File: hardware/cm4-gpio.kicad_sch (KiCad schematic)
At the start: 1 part, among them J2 DF40C-100DP-0.4V_51_

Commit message: Adding SDRAM - missing 3 pins
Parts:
- J2: footprint apparillo-lib:HRS_DF40C-100DP-0.4V_51_ -> ulx5m-gs:HRS_DF40C-100DP-0.4V_51_
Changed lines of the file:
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@@
 			)
 		)
-		(property "Footprint" "apparillo-lib:HRS_DF40C-100DP-0.4V_51_"
+		(property "Footprint" "ulx5m-gs:HRS_DF40C-100DP-0.4V_51_"
 			(at 152.4 88.9 0)
 			(effects

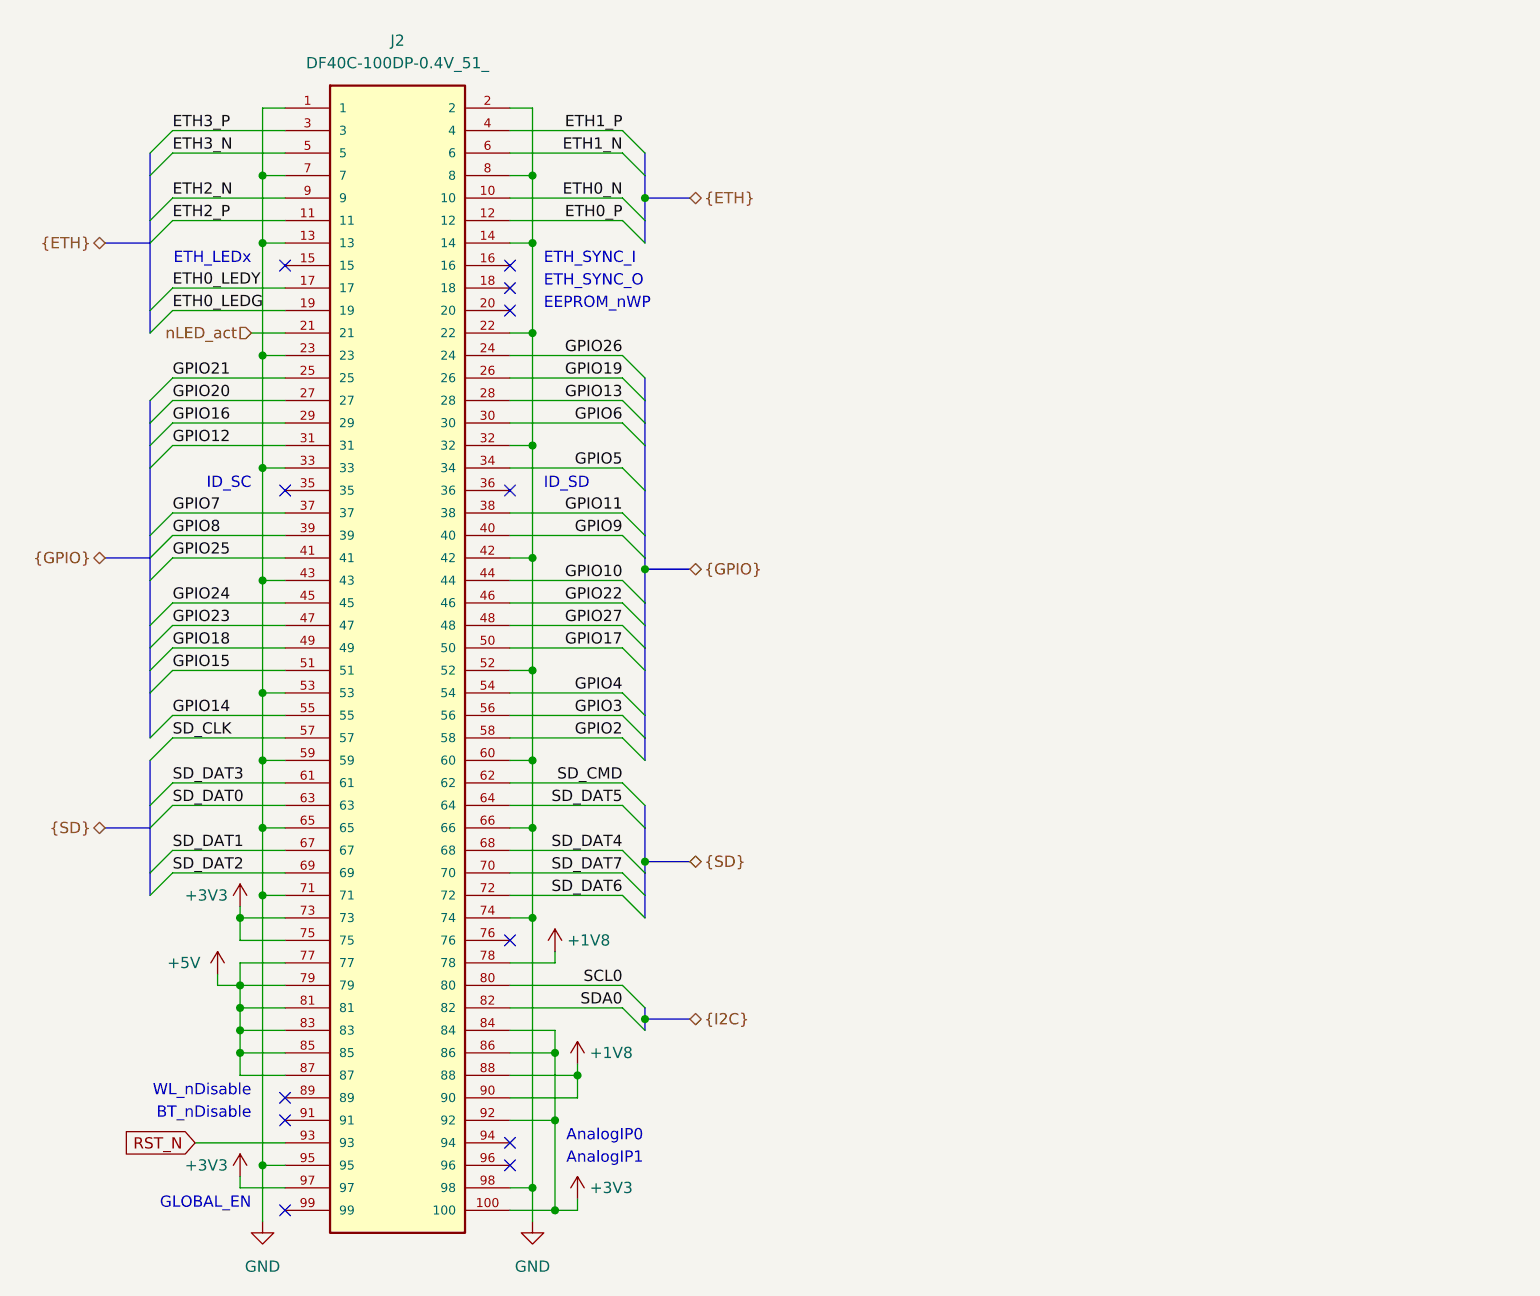
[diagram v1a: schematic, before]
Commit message: Routing diff clock
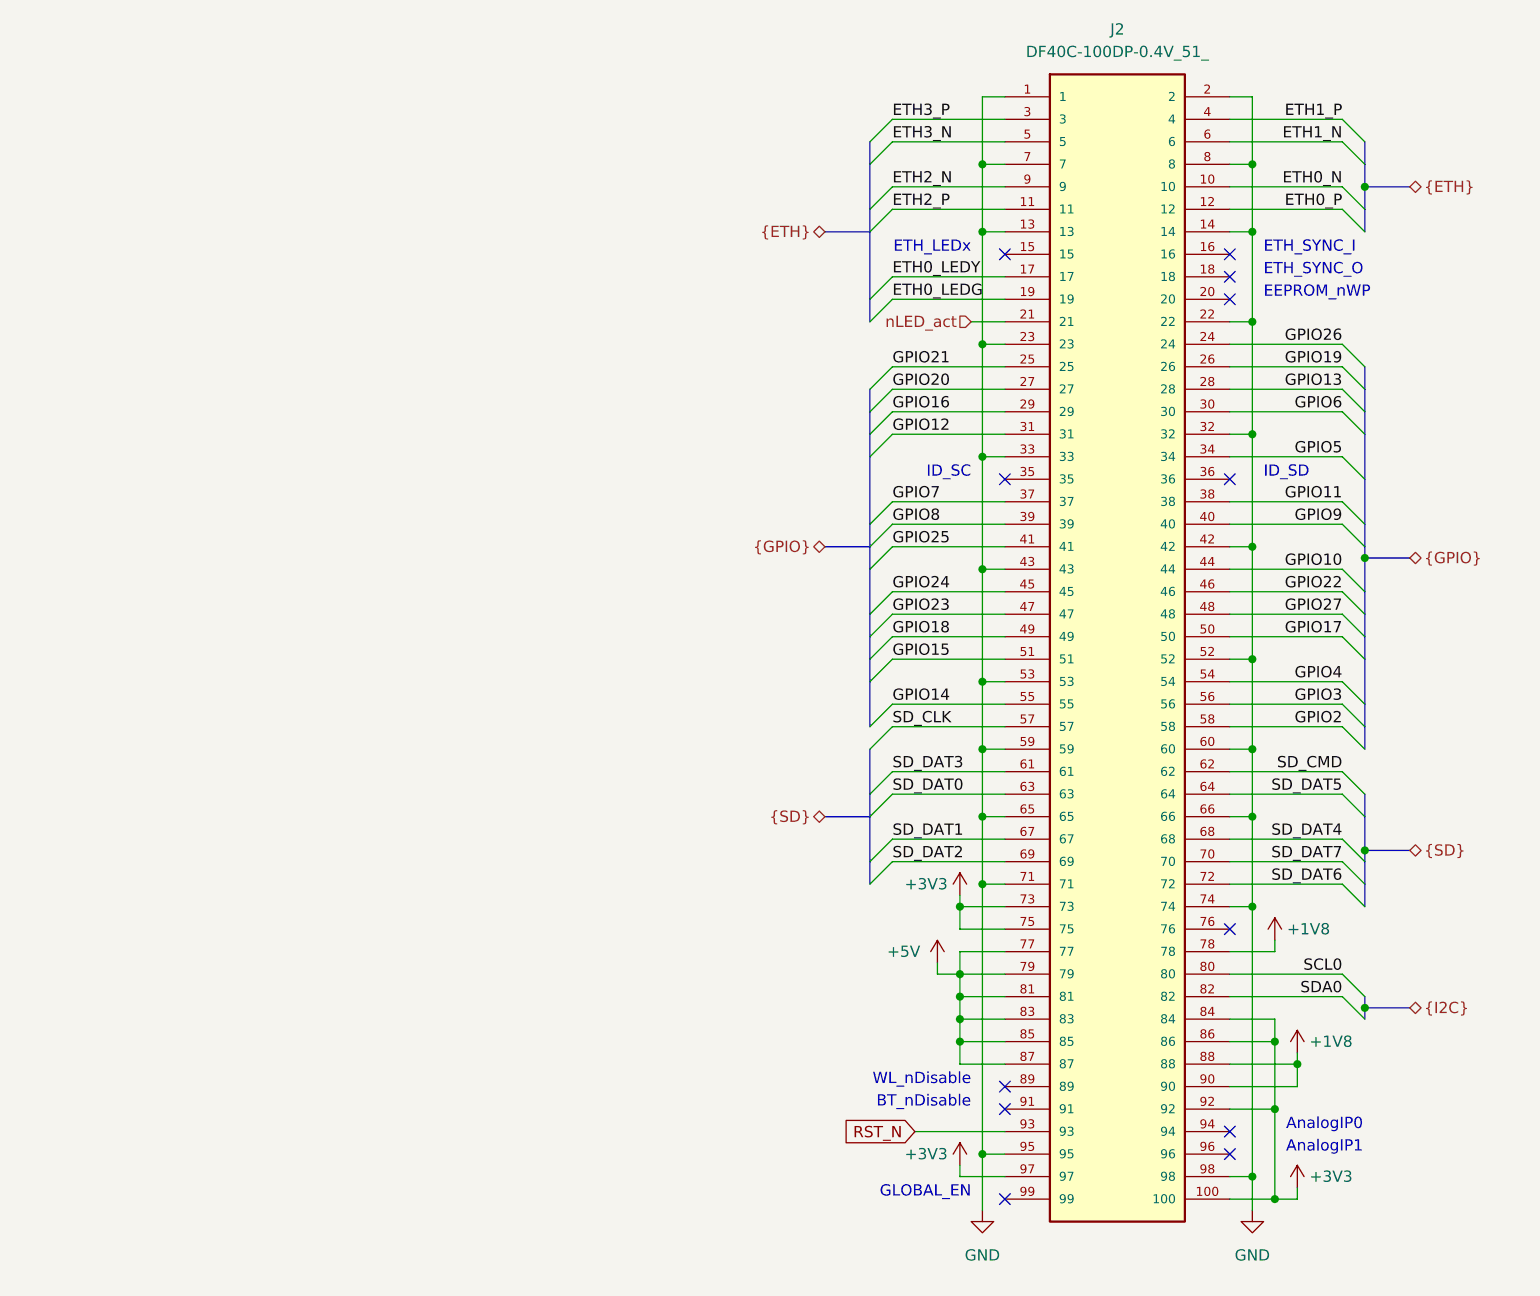
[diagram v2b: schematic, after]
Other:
- company: (none) -> ${project_creator}
- title: (none) -> ${project_name}
- moved on the sheet: J2

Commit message: Routing GPIO
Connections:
- net ID_SC: now reaches J2.35
- net ID_SD: now reaches J2.36
- no-connect marks 12 -> 10
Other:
- note removed: "ID_SC"
- note removed: "ID_SD"

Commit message: Updat to CM5
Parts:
- added R128, R133, R134, R138, R139: 10k, Resistor_SMD:R_0402_1005Metric, symbol Device:R_Small
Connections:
- net +1V8: no longer J2.78
- net +3V3: now also R128.1, R133.1, R134.1, R138.1, R139.2; no longer J2.100, J2.73, J2.75, J2.92, J2.97
- net GND: no longer J2.95
- net ETH_LEDY: now reaches J2.15
- net FAN_TACHO: now reaches J2.16
- net ETH_SYNC_O: now reaches J2.18
- net EEPROM_nWP: now reaches J2.20
- net VBAT: now reaches J2.76
- net USB_CC1: now reaches J2.94
- net USB_CC2: now reaches J2.96
- net at J2.99: now also R133.2
- net ETH0_LEDG renamed FAN_PWM
- net RST_N renamed nRpiBOOT
- new net: J2.100, R139.1
- new net: J2.73, R128.2
- new net: J2.75, R134.2
- new net: J2.97, R138.2
- new net GPIO_VREF: J2.78
- new net LED_nPWR: J2.95
- new net PWR_BTN: J2.92
- no-connect marks 10 -> 2
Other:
- note added: "CAM_GPIO0"
- note added: "PMIC_EN"
- note added: "SD_EN"
- note added: "SD_OVERDRIVE"
- note removed: "AnalogIP0"
- note removed: "AnalogIP1"
- note removed: "EEPROM_nWP"
- note removed: "ETH_LEDx"
- note removed: "ETH_SYNC_I"
- note removed: "ETH_SYNC_O"
- note removed: "GLOBAL_EN"

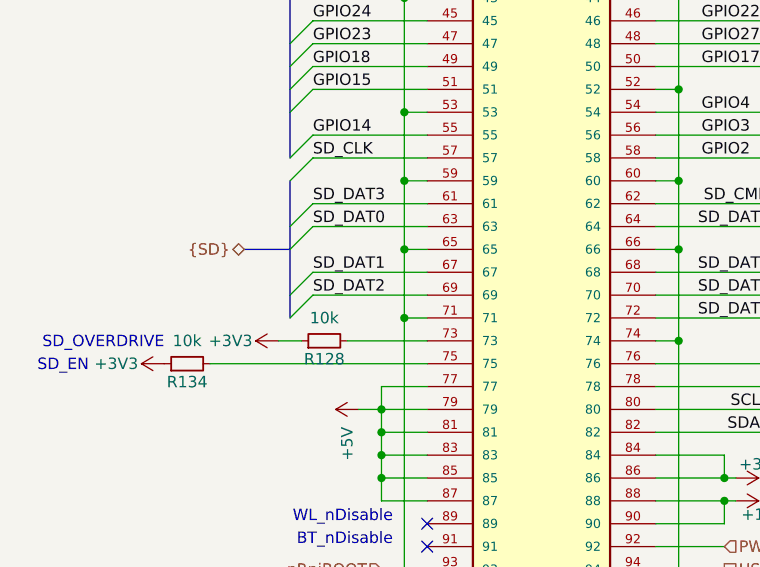
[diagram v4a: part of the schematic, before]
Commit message: Routing GPDI
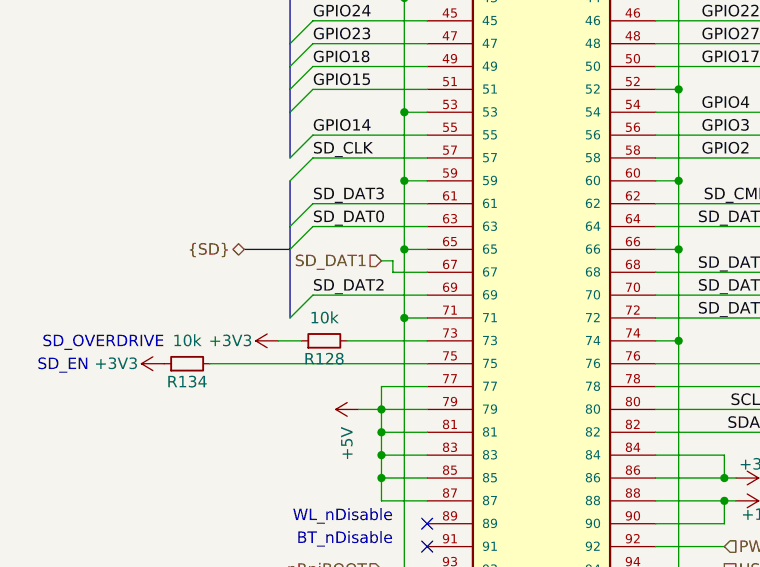
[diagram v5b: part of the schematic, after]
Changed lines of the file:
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@@
-	)
-	(bus_entry
-		(at 208.28 110.49)
-		(size -2.54 2.54)
-		(stroke
-			(width 0)
-			(type default)
-		)
 	)
 	(bus_entry
@@
 		)
 	)
-	(bus
-		(pts
-			(xy 205.74 113.03) (xy 205.74 115.57)
-		)
-		(stroke
-			(width 0)
-			(type default)
-		)
-	)
 	(wire
 		(pts
@@
 	(wire
 		(pts
+			(xy 217.17 109.22) (xy 217.17 110.49)
+		)
+		(stroke
+			(width 0)
+			(type default)
+		)
+	)
+	(wire
+		(pts
 			(xy 246.38 90.17) (xy 248.92 90.17)
 		)
@@
 	(wire
 		(pts
+			(xy 217.17 110.49) (xy 220.98 110.49)
+		)
+		(stroke
+			(width 0)
+			(type default)
+		)
+	)
+	(wire
+		(pts
 			(xy 218.44 54.61) (xy 218.44 67.31)
 		)
@@
 	(wire
 		(pts
-			(xy 208.28 110.49) (xy 220.98 110.49)
+			(xy 215.9 109.22) (xy 217.17 109.22)
 		)
 		(stroke
@@
 	(bus
 		(pts
-			(xy 205.74 107.95) (xy 205.74 113.03)
+			(xy 205.74 107.95) (xy 205.74 115.57)
 		)
 		(stroke
@@
 	(label "GPIO25"
 		(at 208.28 77.47 0)
-		(effects
-			(font
-				(size 1.27 1.27)
-			)
-			(justify left bottom)
-		)
-	)
-	(label "SD_DAT1"
-		(at 208.28 110.49 0)
 		(effects
 			(font
@@
 		(effects
 			(font
+				(size 1.27 1.27)
+			)
+			(justify right)
+		)
+	)
+	(hierarchical_label "SD_DAT1"
+		(shape input)
+		(at 215.9 109.22 180)
+		(effects
+			(font

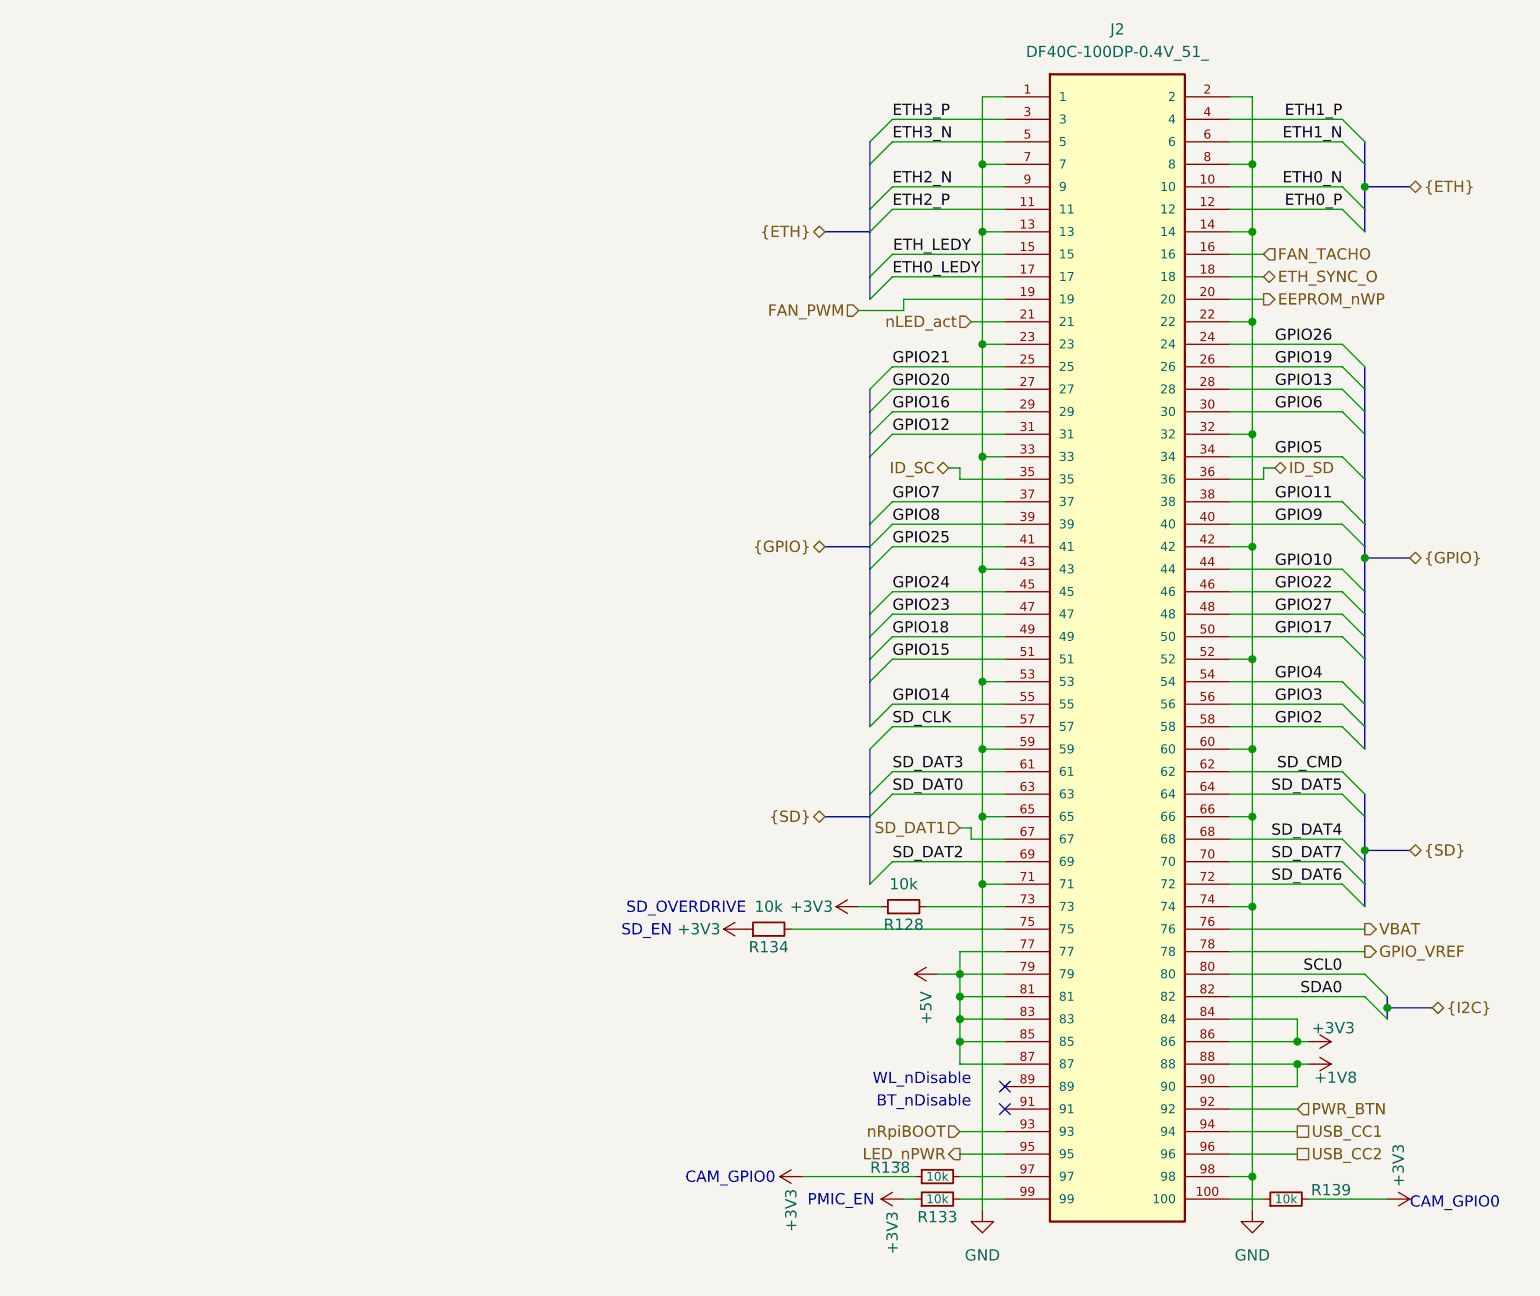
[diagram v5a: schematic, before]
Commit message: Clearing ERC errors/warnings
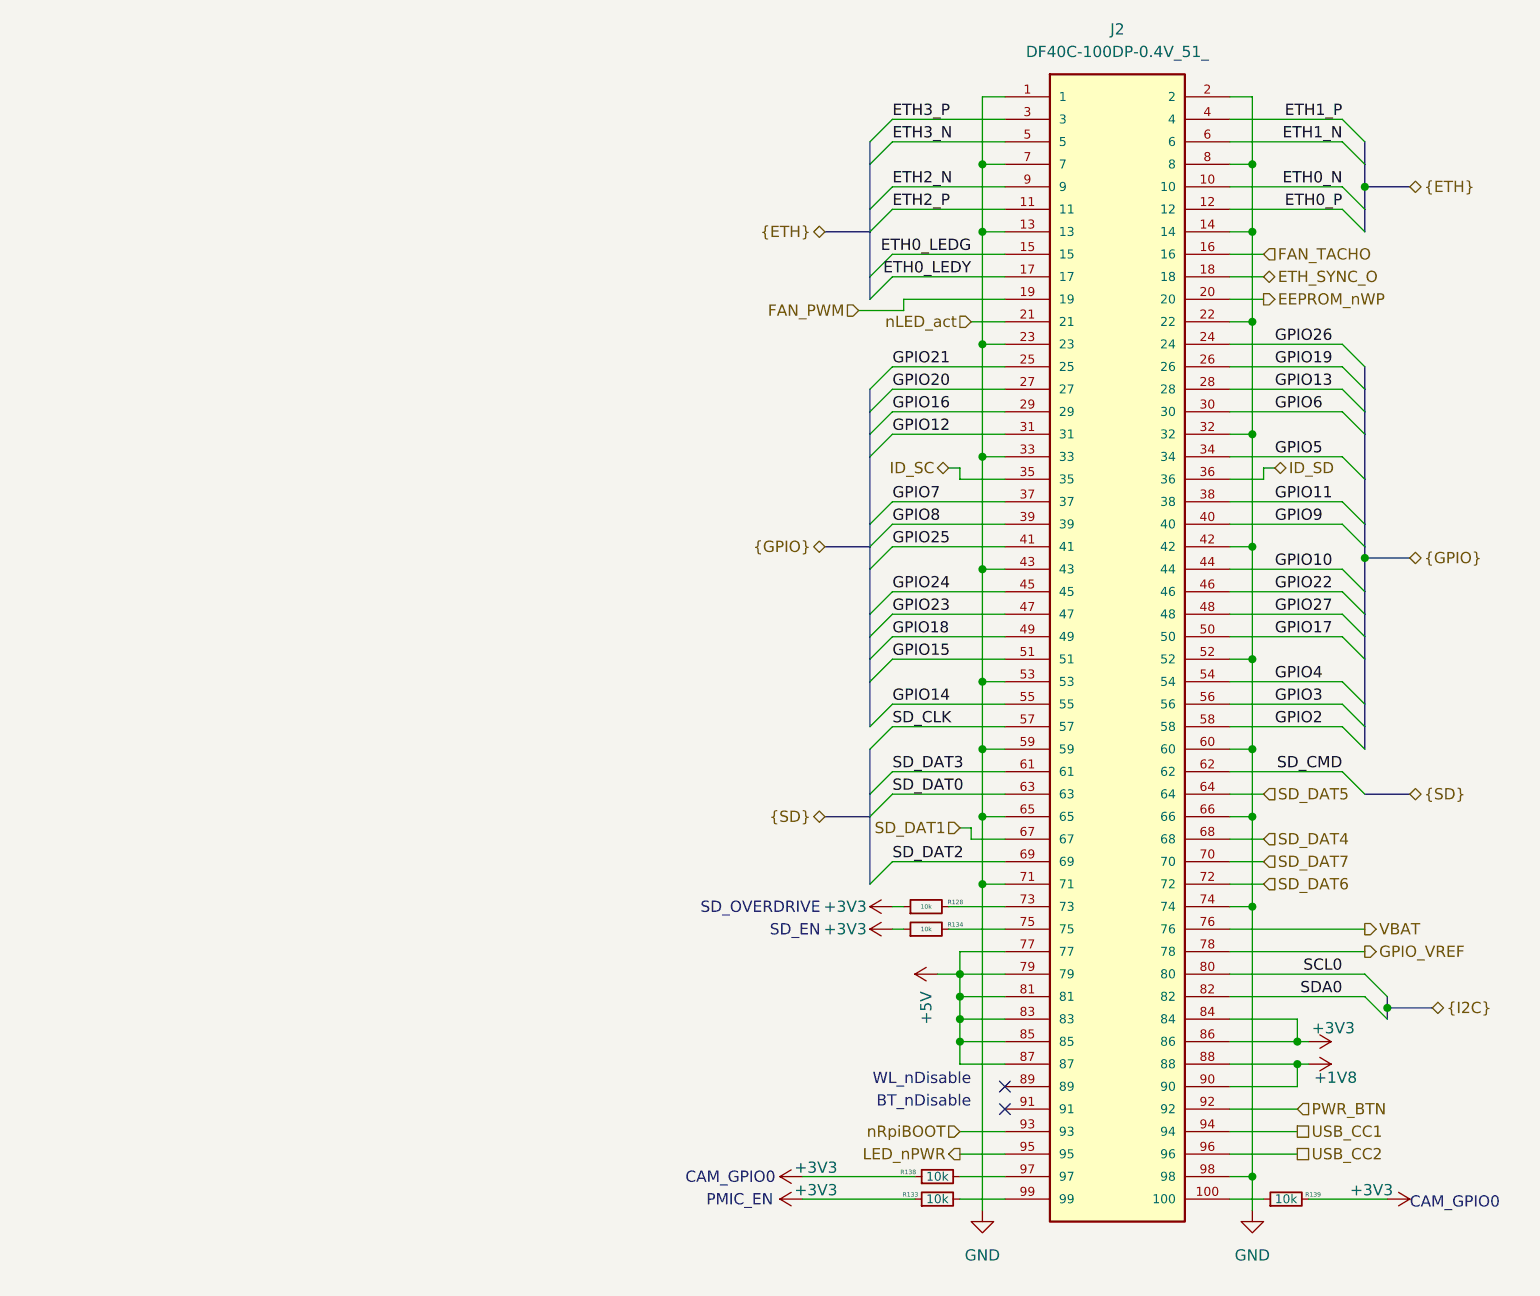
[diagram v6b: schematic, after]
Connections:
- net ETH_LEDY renamed ETH0_LEDG
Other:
- moved on the sheet: R128, R134
